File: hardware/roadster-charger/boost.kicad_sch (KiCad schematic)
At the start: 29 parts, among them U10 DAC70501ZDQFT, U12 PI3740-00-LGIZ

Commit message: change all 1K Rs to 0.1%, invert DAC jumpers
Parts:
- removed JP1: SolderJumper_2_Bridged, Jumper:SolderJumper-2_P1.3mm_Bridged2Bar_RoundedPad1.0x1.5mm, symbol Jumper:SolderJumper_2_Bridged
- added JP1: SolderJumper_2_Open, Jumper:SolderJumper-2_P1.3mm_Open_RoundedPad1.0x1.5mm, symbol Jumper:SolderJumper_2_Open
- R23: MPN RC0603FR-071KL -> RT0603BRD071KL
- R25: MPN DNP -> RT0603BRD071KL; now fitted
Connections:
- net at U10.2 (VOUT): now also R25.1, JP1.2 (B); no longer R25.2
- net at C18.1, TP8.1, U12.A6 (TRK): now also R25.2, JP1.1 (A); no longer R25.1
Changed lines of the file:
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@@
-	)
-	(symbol
-		(lib_id "Jumper:SolderJumper_2_Bridged")
-		(at 175.26 138.43 0)
-		(unit 1)
-		(exclude_from_sim yes)
-		(in_bom no)
-		(on_board yes)
-		(dnp no)
-		(property "Reference" "JP1"
-			(at 175.26 141.224 0)
-			(effects
-				(font
-					(size 1.27 1.27)
-				)
-			)
-		)
-		(property "Value" "SolderJumper_2_Bridged"
-			(at 175.26 141.732 0)
-			(effects
-				(font
-					(size 1.27 1.27)
-				)
-				(hide yes)
-			)
-		)
-		(property "Footprint" "Jumper:SolderJumper-2_P1.3mm_Bridged2Bar_RoundedPad1.0x1.5mm"
-			(at 175.26 138.43 0)
-			(effects
-				(font
-					(size 1.27 1.27)
-				)
-				(hide yes)
-			)
-		)
-		(property "Datasheet" "~"
-			(at 175.26 138.43 0)
-			(effects
-				(font
-					(size 1.27 1.27)
-				)
-				(hide yes)
-			)
-		)
-		(property "Description" "Solder Jumper, 2-pole, closed/bridged"
-			(at 175.26 138.43 0)
-			(effects
-				(font
-					(size 1.27 1.27)
-				)
-				(hide yes)
-			)
-		)
-		(pin "1"
-		)
-		(pin "2"
-		)
-		(instances
-			(project ""
-				(path "/57ecac41-cd8a-4182-a81e-fed3e381aedd/64ca4e4e-11ba-4e5c-8f8e-2432a1d47dd0"
-					(reference "JP1")
-					(unit 1)
-				)
-			)
-		)
 	)
 	(symbol
@@
 	)
 	(symbol
+		(lib_id "Device:R_Small")
+		(at 175.26 134.62 90)
+		(mirror x)
+		(unit 1)
+		(exclude_from_sim no)
+		(in_bom yes)
+		(on_board yes)
+		(dnp no)
+		(property "Reference" "R25"
+			(at 171.704 132.334 90)
+			(effects
+				(font
+					(size 1.27 1.27)
+				)
+				(justify right)
+			)
+		)
+		(property "Value" "1K"
+			(at 176.276 132.334 90)
+			(effects
+				(font
+					(size 1.27 1.27)
+				)
+				(justify right)
+			)
+		)
+		(property "Footprint" "Resistor_SMD:R_0603_1608Metric"
+			(at 175.26 134.62 0)
+			(effects
+				(font
+					(size 1.27 1.27)
+				)
+				(hide yes)
+			)
+		)
+		(property "Datasheet" "~"
+			(at 175.26 134.62 0)
+			(effects
+				(font
+					(size 1.27 1.27)
+				)
+				(hide yes)
+			)
+		)
+		(property "Description" ""
+			(at 175.26 134.62 0)
+			(effects
+				(font
+					(size 1.27 1.27)
+				)
+				(hide yes)
+			)
+		)
+		(property "MPN" "RT0603BRD071KL"
+			(at 175.26 134.62 0)
+			(effects
+				(font
+					(size 1.27 1.27)
+				)
+				(hide yes)
+			)
+		)
+		(pin "1"
+		)
+		(pin "2"
+		)
+		(instances
+			(project "roadster-charger"
+				(path "/57ecac41-cd8a-4182-a81e-fed3e381aedd/64ca4e4e-11ba-4e5c-8f8e-2432a1d47dd0"
+					(reference "R25")
+					(unit 1)
+				)
+			)
+		)
+	)
+	(symbol
 		(lib_id "Connector:TestPoint")
 		(at 248.92 102.87 0)
@@
 			)
 		)
-		(property "MPN" "RC0603FR-071KL"
+		(property "MPN" "RT0603BRD071KL"
 			(at 242.57 116.84 0)
 			(effects
@@
 	)
 	(symbol
+		(lib_id "Jumper:SolderJumper_2_Open")
+		(at 175.26 138.43 180)
+		(unit 1)
+		(exclude_from_sim yes)
+		(in_bom no)
+		(on_board yes)
+		(dnp no)
+		(property "Reference" "JP1"
+			(at 175.26 141.224 0)
+			(effects
+				(font
+					(size 1.27 1.27)
+				)
+			)
+		)
+		(property "Value" "SolderJumper_2_Open"
+			(at 175.26 142.24 0)
+			(effects
+				(font
+					(size 1.27 1.27)
+				)
+				(hide yes)
+			)
+		)
+		(property "Footprint" "Jumper:SolderJumper-2_P1.3mm_Open_RoundedPad1.0x1.5mm"
+			(at 175.26 138.43 0)
+			(effects
+				(font
+					(size 1.27 1.27)
+				)
+				(hide yes)
+			)
+		)
+		(property "Datasheet" "~"
+			(at 175.26 138.43 0)
+			(effects
+				(font
+					(size 1.27 1.27)
+				)
+				(hide yes)
+			)
+		)
+		(property "Description" "Solder Jumper, 2-pole, open"
+			(at 175.26 138.43 0)
+			(effects
+				(font
+					(size 1.27 1.27)
+				)
+				(hide yes)
+			)
+		)
+		(pin "1"
+		)
+		(pin "2"
+		)
+		(instances
+			(project ""
+				(path "/57ecac41-cd8a-4182-a81e-fed3e381aedd/64ca4e4e-11ba-4e5c-8f8e-2432a1d47dd0"
+					(reference "JP1")
+					(unit 1)
+				)
+			)
+		)
+	)
+	(symbol
 		(lib_id "power:+3.3V")
 		(at 115.57 129.54 0)
@@
 					(unit 1)
 				)
-			)
-		)
-	)
-	(symbol
-		(lib_id "Device:R_Small")
-		(at 175.26 134.62 270)
-		(unit 1)
-		(exclude_from_sim no)
-		(in_bom yes)
-		(on_board yes)
-		(dnp yes)
-		(property "Reference" "R25"
-			(at 179.07 131.826 90)
-			(effects
-				(font
-					(size 1.27 1.27)
-				)
-				(justify right)
-			)
-		)
-		(property "Value" "1K"
-			(at 173.736 131.826 90)
-			(effects
-				(font
-					(size 1.27 1.27)
-				)
-				(justify right)
-			)
-		)
-		(property "Footprint" "Resistor_SMD:R_0603_1608Metric"
-			(at 175.26 134.62 0)
-			(effects
-				(font
-					(size 1.27 1.27)
-				)
-				(hide yes)
-			)
-		)
-		(property "Datasheet" "~"
-			(at 175.26 134.62 0)
-			(effects
-				(font
-					(size 1.27 1.27)
-				)
-				(hide yes)
-			)
-		)
-		(property "Description" ""
-			(at 175.26 134.62 0)
-			(effects
-				(font
-					(size 1.27 1.27)
-				)
-				(hide yes)
-			)
-		)
-		(property "MPN" "DNP"
-			(at 175.26 134.62 0)
-			(effects
-				(font
-					(size 1.27 1.27)
-				)
-				(hide yes)
-			)
-		)
-		(pin "1"
-		)
-		(pin "2"
-		)
-		(instances
-			(project "roadster-charger"
-				(path "/57ecac41-cd8a-4182-a81e-fed3e381aedd/64ca4e4e-11ba-4e5c-8f8e-2432a1d47dd0"
-					(reference "R25")
-					(unit 1)
-				)

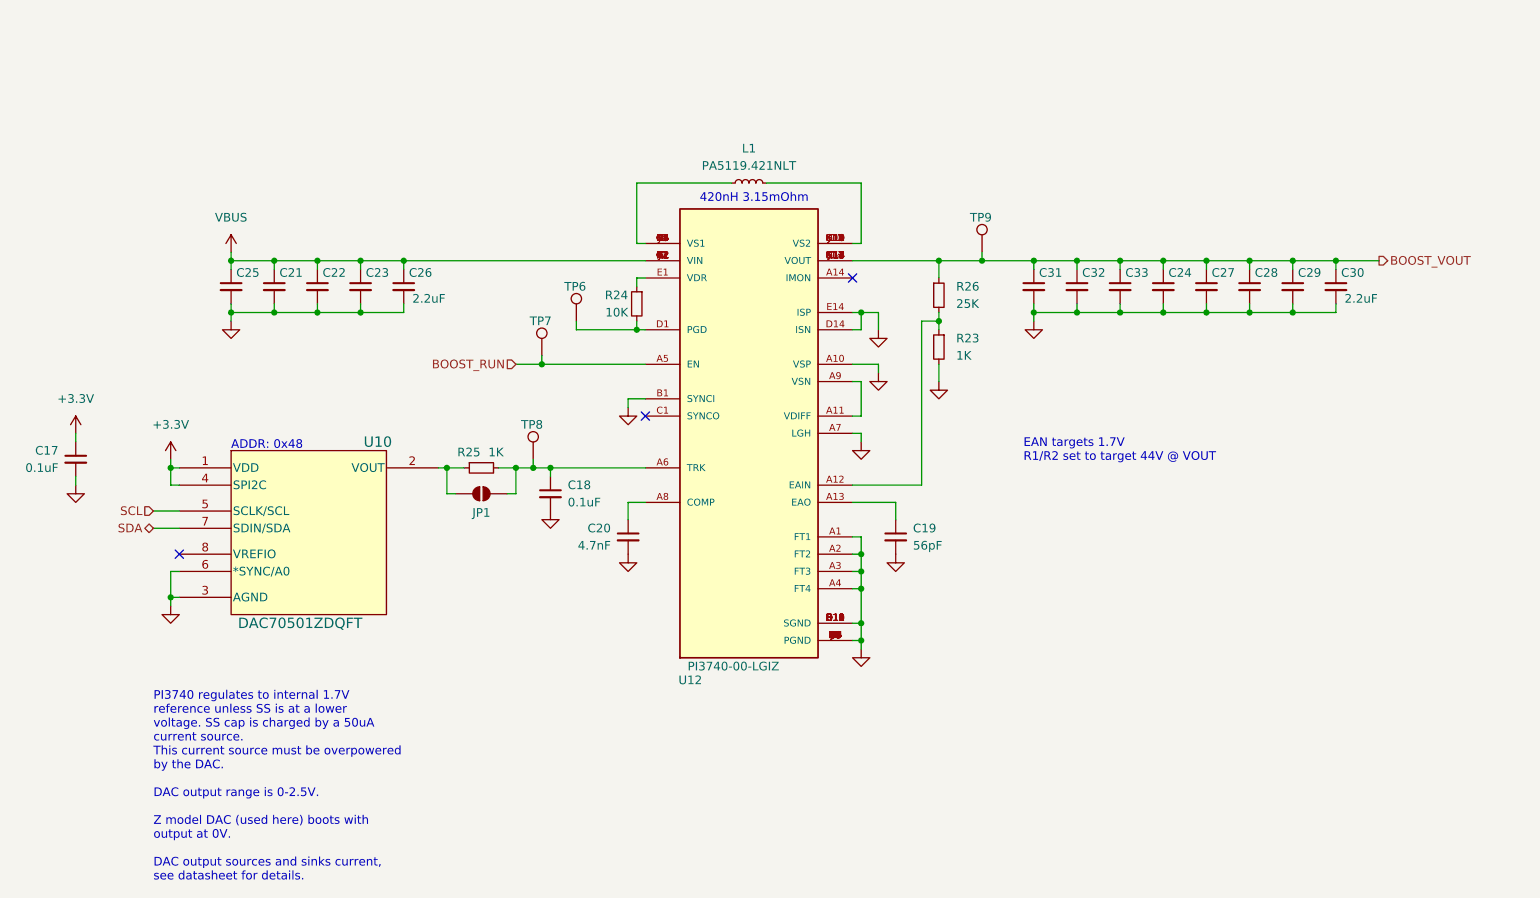
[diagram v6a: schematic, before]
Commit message: reannotate, add uart test points
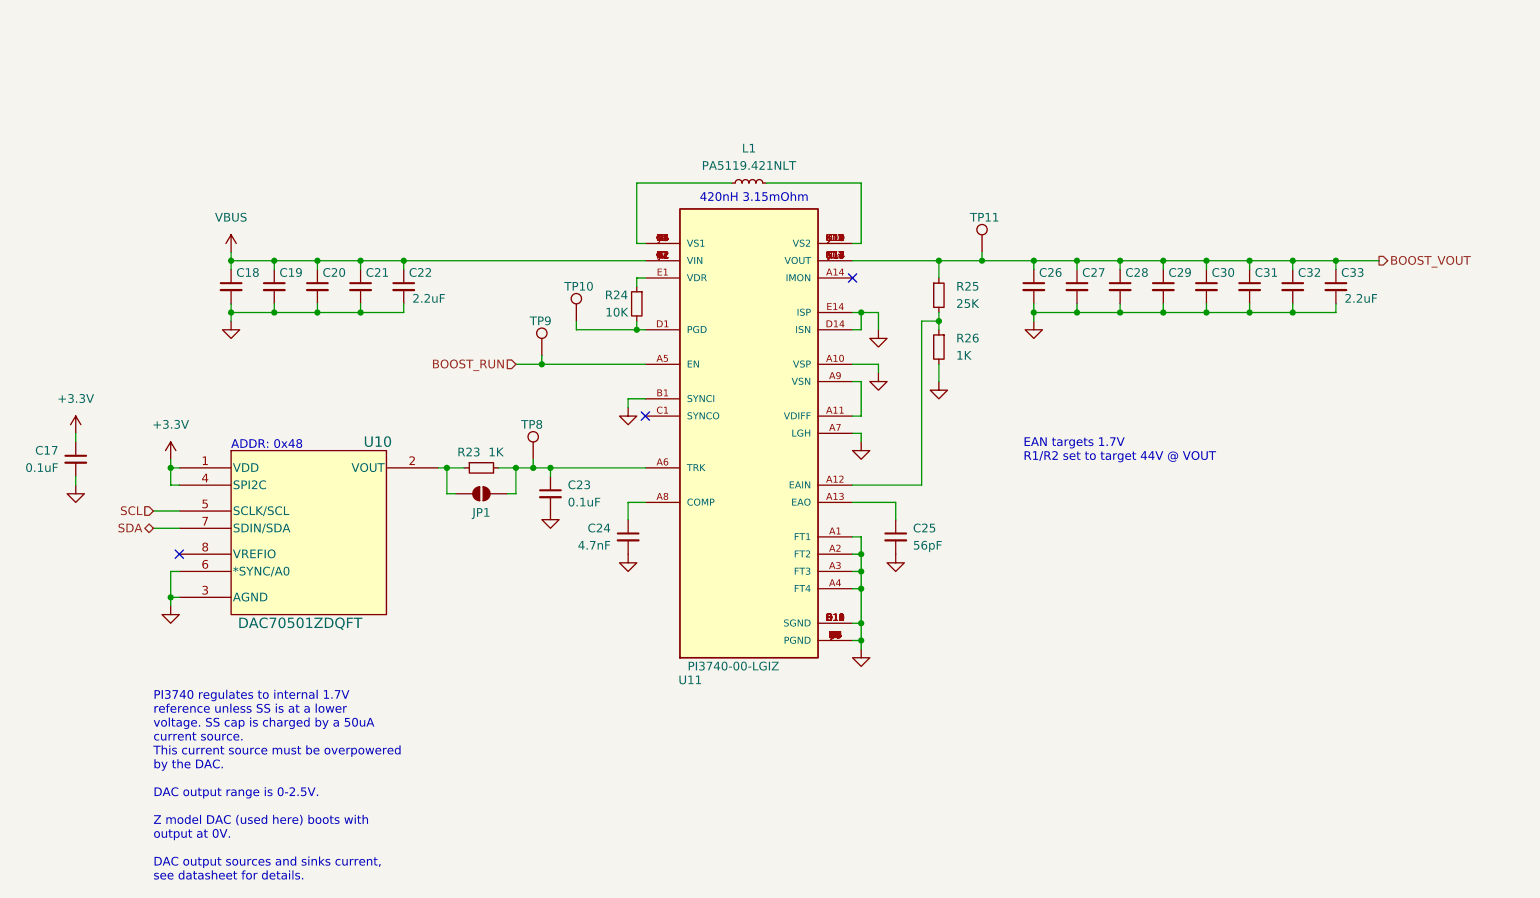
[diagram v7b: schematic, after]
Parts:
- renumbered C25 to C18, C21 to C19, C22 to C20, C23 to C21, C26 to C22, C18 to C23, C20 to C24, C19 to C25, C31 to C26, C32 to C27, C33 to C28, C24 to C29, C27 to C30, C28 to C31, C29 to C32, C30 to C33, R25 to R23, R26 to R25, R23 to R26, TP6 to TP10, TP9 to TP11, TP7 to TP9, U12 to U11

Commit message: Correct Vicor grounding and redo boost layout
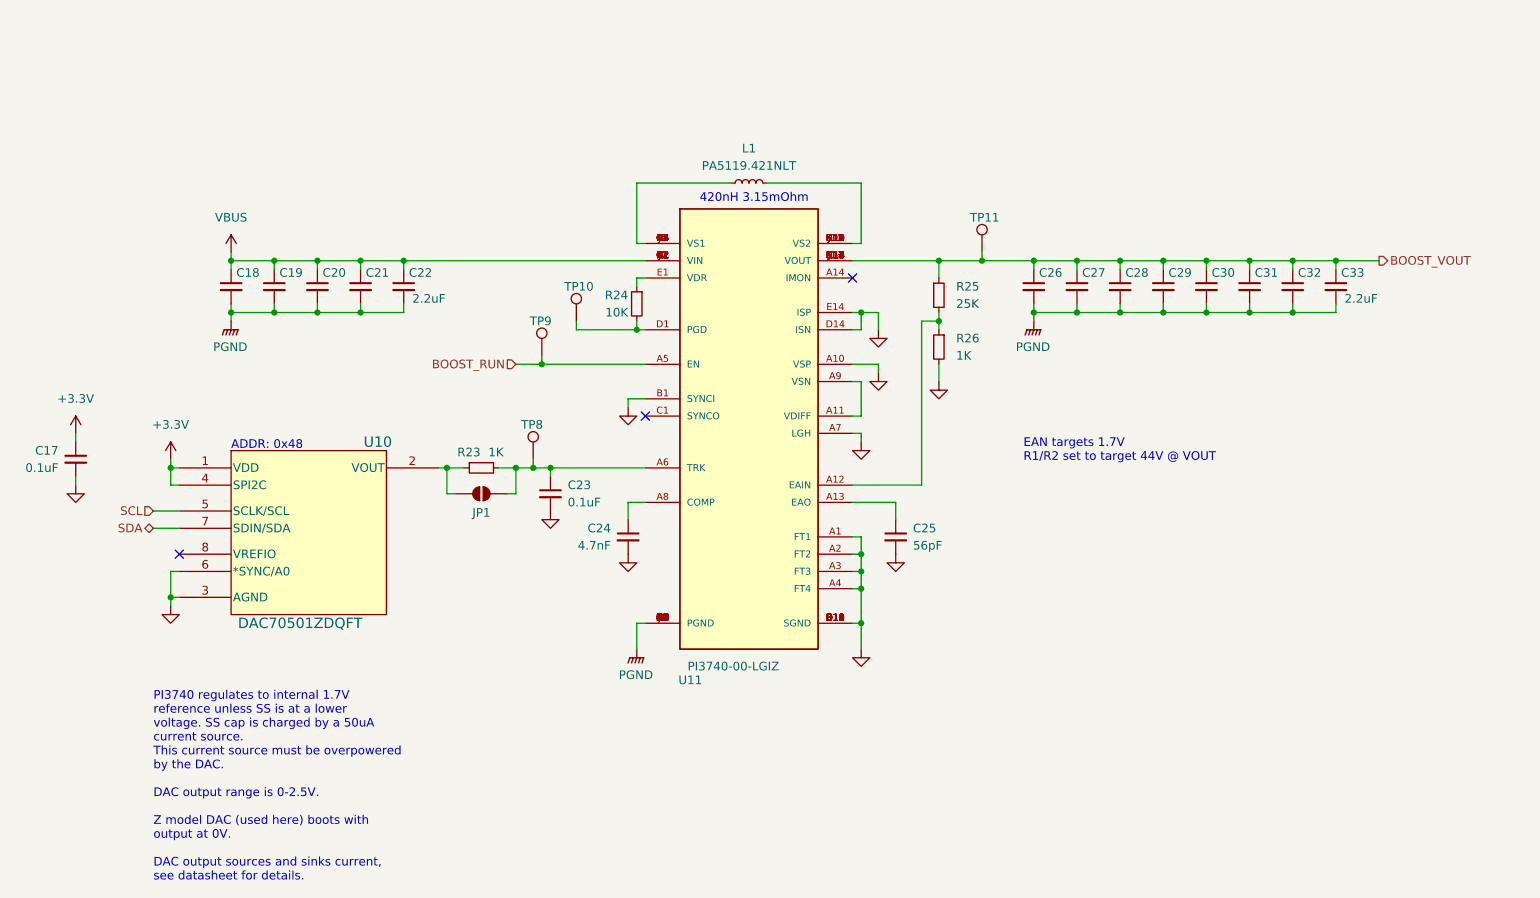
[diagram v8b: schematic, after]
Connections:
- net GND: no longer C18.2, C19.2, C20.2, C21.2, C22.2, C26.2, C27.2, C28.2, C29.2, C30.2, C31.2, C32.2, C33.2, U11.B2 (PGND), U11.B3 (PGND), U11.B4 (PGND), U11.B5 (PGND), U11.B6 (PGND), U11.B7 (PGND), U11.B8 (PGND), U11.B9 (PGND), U11.C2 (PGND), U11.C3 (PGND), U11.C4 (PGND), U11.C5 (PGND), U11.C6 (PGND), U11.C7 (PGND), U11.C8 (PGND), U11.C9 (PGND), U11.D2 (PGND), U11.D3 (PGND), U11.D4 (PGND), U11.D5 (PGND), U11.D6 (PGND), U11.D7 (PGND), U11.D8 (PGND), U11.D9 (PGND), U11.E2 (PGND), U11.E3 (PGND), U11.E4 (PGND), U11.E5 (PGND), U11.E6 (PGND), U11.E7 (PGND), U11.E8 (PGND), U11.E9 (PGND), U11.F7 (PGND), U11.F8 (PGND), U11.G7 (PGND), U11.G8 (PGND), U11.H7 (PGND), U11.H8 (PGND), U11.J7 (PGND), U11.J8 (PGND), U11.K7 (PGND), U11.K8 (PGND)
- new net PGND: C18.2, C19.2, C20.2, C21.2, C22.2, C26.2, C27.2, C28.2, C29.2, C30.2, C31.2, C32.2, C33.2, U11.B2 (PGND), U11.B3 (PGND), U11.B4 (PGND), U11.B5 (PGND), U11.B6 (PGND), U11.B7 (PGND), U11.B8 (PGND), U11.B9 (PGND), U11.C2 (PGND), U11.C3 (PGND), U11.C4 (PGND), U11.C5 (PGND), U11.C6 (PGND), U11.C7 (PGND), U11.C8 (PGND), U11.C9 (PGND), U11.D2 (PGND), U11.D3 (PGND), U11.D4 (PGND), U11.D5 (PGND), U11.D6 (PGND), U11.D7 (PGND), U11.D8 (PGND), U11.D9 (PGND), U11.E2 (PGND), U11.E3 (PGND), U11.E4 (PGND), U11.E5 (PGND), U11.E6 (PGND), U11.E7 (PGND), U11.E8 (PGND), U11.E9 (PGND), U11.F7 (PGND), U11.F8 (PGND), U11.G7 (PGND), U11.G8 (PGND), U11.H7 (PGND), U11.H8 (PGND), U11.J7 (PGND), U11.J8 (PGND), U11.K7 (PGND), U11.K8 (PGND)
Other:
- moved on the sheet: U11
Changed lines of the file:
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@@
-	)
-	(junction
-		(at 231.14 160.02)
-		(diameter 0)
-		(color 0 0 0 0)
 	)
 	(junction
@@
 	(wire
 		(pts
+			(xy 198.12 157.48) (xy 198.12 161.29)
+		)
+		(stroke
+			(width 0)
+			(type default)
+		)
+	)
+	(wire
+		(pts
 			(xy 281.94 104.14) (xy 288.29 104.14)
 		)
@@
 	(wire
 		(pts
-			(xy 231.14 157.48) (xy 231.14 160.02)
-		)
-		(stroke
-			(width 0)
-			(type default)
-		)
-	)
-	(wire
-		(pts
 			(xy 229.87 104.14) (xy 242.57 104.14)
 		)
@@
 	(wire
 		(pts
-			(xy 229.87 160.02) (xy 231.14 160.02)
-		)
-		(stroke
-			(width 0)
-			(type default)
-		)
-	)
-	(wire
-		(pts
 			(xy 240.03 137.16) (xy 229.87 137.16)
 		)
@@
 	(wire
 		(pts
-			(xy 231.14 160.02) (xy 231.14 161.29)
+			(xy 231.14 157.48) (xy 231.14 161.29)
 		)
 		(stroke
@@
 		(pts
 			(xy 198.12 106.68) (xy 199.39 106.68)
+		)
+		(stroke
+			(width 0)
+			(type default)
+		)
+	)
+	(wire
+		(pts
+			(xy 199.39 157.48) (xy 198.12 157.48)
 		)
 		(stroke
@@
 	)
 	(symbol
-		(lib_id "power:GND")
-		(at 256.54 113.03 0)
-		(unit 1)
-		(exclude_from_sim no)
-		(in_bom yes)
-		(on_board yes)
-		(dnp no)
-		(property "Reference" "#PWR088"
-			(at 256.54 119.38 0)
-			(effects
-				(font
-					(size 1.27 1.27)
-				)
-				(hide yes)
-			)
-		)
-		(property "Value" "GND"
-			(at 256.54 118.11 0)
-			(effects
-				(font
-					(size 1.27 1.27)
-				)
-				(hide yes)
-			)
-		)
-		(property "Footprint" ""
-			(at 256.54 113.03 0)
-			(effects
-				(font
-					(size 1.27 1.27)
-				)
-				(hide yes)
-			)
-		)
-		(property "Datasheet" ""
-			(at 256.54 113.03 0)
-			(effects
-				(font
-					(size 1.27 1.27)
-				)
-				(hide yes)
-			)
-		)
-		(property "Description" ""
-			(at 256.54 113.03 0)
-			(effects
-				(font
-					(size 1.27 1.27)
-				)
-				(hide yes)
-			)
-		)
-		(pin "1"
-		)
-		(instances
-			(project "roadster-charger"
-				(path "/57ecac41-cd8a-4182-a81e-fed3e381aedd/64ca4e4e-11ba-4e5c-8f8e-2432a1d47dd0"
-					(reference "#PWR088")
-					(unit 1)
-				)
-			)
-		)
-	)
-	(symbol
 		(lib_id "DAC70501:DAC70501MDQFR")
 		(at 130.81 138.43 0)
@@
 	)
 	(symbol
+		(lib_id "power:GNDPWR")
+		(at 138.43 113.03 0)
+		(unit 1)
+		(exclude_from_sim no)
+		(in_bom yes)
+		(on_board yes)
+		(dnp no)
+		(property "Reference" "#PWR078"
+			(at 138.43 118.11 0)
+			(effects
+				(font
+					(size 1.27 1.27)
+				)
+				(hide yes)
+			)
+		)
+		(property "Value" "PGND"
+			(at 138.303 116.84 0)
+			(effects
+				(font
+					(size 1.27 1.27)
+				)
+			)
+		)
+		(property "Footprint" ""
+			(at 138.43 114.3 0)
+			(effects
+				(font
+					(size 1.27 1.27)
+				)
+				(hide yes)
+			)
+		)
+		(property "Datasheet" ""
+			(at 138.43 114.3 0)
+			(effects
+				(font
+					(size 1.27 1.27)
+				)
+				(hide yes)
+			)
+		)
+		(property "Description" "Power symbol creates a global label with name \"GNDPWR\" , global ground"
+			(at 138.43 113.03 0)
+			(effects
+				(font
+					(size 1.27 1.27)
+				)
+				(hide yes)
+			)
+		)
+		(pin "1"
+		)
+		(instances
+			(project ""
+				(path "/57ecac41-cd8a-4182-a81e-fed3e381aedd/64ca4e4e-11ba-4e5c-8f8e-2432a1d47dd0"
+					(reference "#PWR078")
+					(unit 1)
+				)
+			)
+		)
+	)
+	(symbol
 		(lib_id "Device:C_Small")
 		(at 262.89 107.95 0)
@@
 	)
 	(symbol
-		(lib_id "power:GND")
-		(at 138.43 113.03 0)
+		(lib_id "power:GNDPWR")
+		(at 198.12 161.29 0)
 		(unit 1)
 		(exclude_from_sim no)
@@
 		(on_board yes)
 		(dnp no)
-		(property "Reference" "#PWR078"
-			(at 138.43 119.38 0)
-			(effects
-				(font
-					(size 1.27 1.27)
-				)
-				(hide yes)
-			)
-		)
-		(property "Value" "GND"
-			(at 138.43 118.11 0)
-			(effects
-				(font
-					(size 1.27 1.27)
-				)
-				(hide yes)
+		(property "Reference" "#PWR089"
+			(at 198.12 166.37 0)
+			(effects
+				(font
+					(size 1.27 1.27)
+				)
+				(hide yes)
+			)
+		)
+		(property "Value" "PGND"
+			(at 197.993 165.1 0)
+			(effects
+				(font
+					(size 1.27 1.27)
+				)
 			)
 		)
 		(property "Footprint" ""
-			(at 138.43 113.03 0)
+			(at 198.12 162.56 0)
 			(effects
 				(font
@@
 		)
 		(property "Datasheet" ""
-			(at 138.43 113.03 0)
-			(effects
-				(font
-					(size 1.27 1.27)
-				)
-				(hide yes)
-			)
-		)
-		(property "Description" ""
-			(at 138.43 113.03 0)
+			(at 198.12 162.56 0)
+			(effects
+				(font
+					(size 1.27 1.27)
+				)
+				(hide yes)
+			)
+		)
+		(property "Description" "Power symbol creates a global label with name \"GNDPWR\" , global ground"
+			(at 198.12 161.29 0)
 			(effects
 				(font
@@
 			(project "roadster-charger"
 				(path "/57ecac41-cd8a-4182-a81e-fed3e381aedd/64ca4e4e-11ba-4e5c-8f8e-2432a1d47dd0"
-					(reference "#PWR078")
+					(reference "#PWR089")
 					(unit 1)
 				)
@@
 					(unit 1)
 				)
+			)
+		)
+	)
+	(symbol
+		(lib_id "power:GNDPWR")
+		(at 256.54 113.03 0)
+		(unit 1)
+		(exclude_from_sim no)
+		(in_bom yes)
+		(on_board yes)
+		(dnp no)
+		(property "Reference" "#PWR088"
+			(at 256.54 118.11 0)
+			(effects
+				(font
+					(size 1.27 1.27)
+				)
+				(hide yes)
+			)
+		)
+		(property "Value" "PGND"
+			(at 256.413 116.84 0)
+			(effects
+				(font
+					(size 1.27 1.27)
+				)
+			)
+		)
+		(property "Footprint" ""
+			(at 256.54 114.3 0)
+			(effects
+				(font
+					(size 1.27 1.27)
+				)
+				(hide yes)
+			)
+		)
+		(property "Datasheet" ""
+			(at 256.54 114.3 0)
+			(effects
+				(font
+					(size 1.27 1.27)
+				)
+				(hide yes)
+			)
+		)
+		(property "Description" "Power symbol creates a global label with name \"GNDPWR\" , global ground"
+			(at 256.54 113.03 0)
+			(effects
+				(font
+					(size 1.27 1.27)
+				)
+				(hide yes)
+			)
+		)
+		(pin "1"
+		)
+		(instances
+			(project "roadster-charger"
+				(path "/57ecac41-cd8a-4182-a81e-fed3e381aedd/64ca4e4e-11ba-4e5c-8f8e-2432a1d47dd0"
+					(reference "#PWR088")
+					(unit 1)
+				)
